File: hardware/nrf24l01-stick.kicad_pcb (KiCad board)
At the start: 2 copper layers, 48.3 x 16.3 mm, 25 parts, among them J1 USB_B_Micro, J2 SWD, SW1 SW_Push, U1 STM32L082KBUx, U2 NRF24L01_Breakout, U3 LP2985-3.3

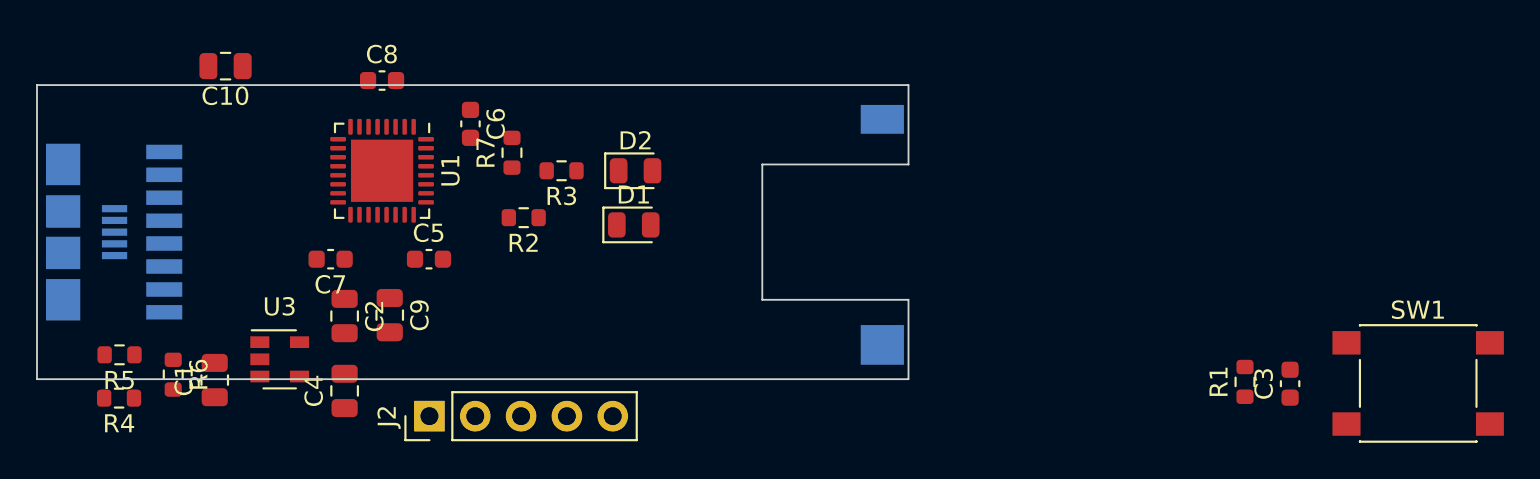
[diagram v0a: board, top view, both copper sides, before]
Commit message: Designed the rest of the PCB.
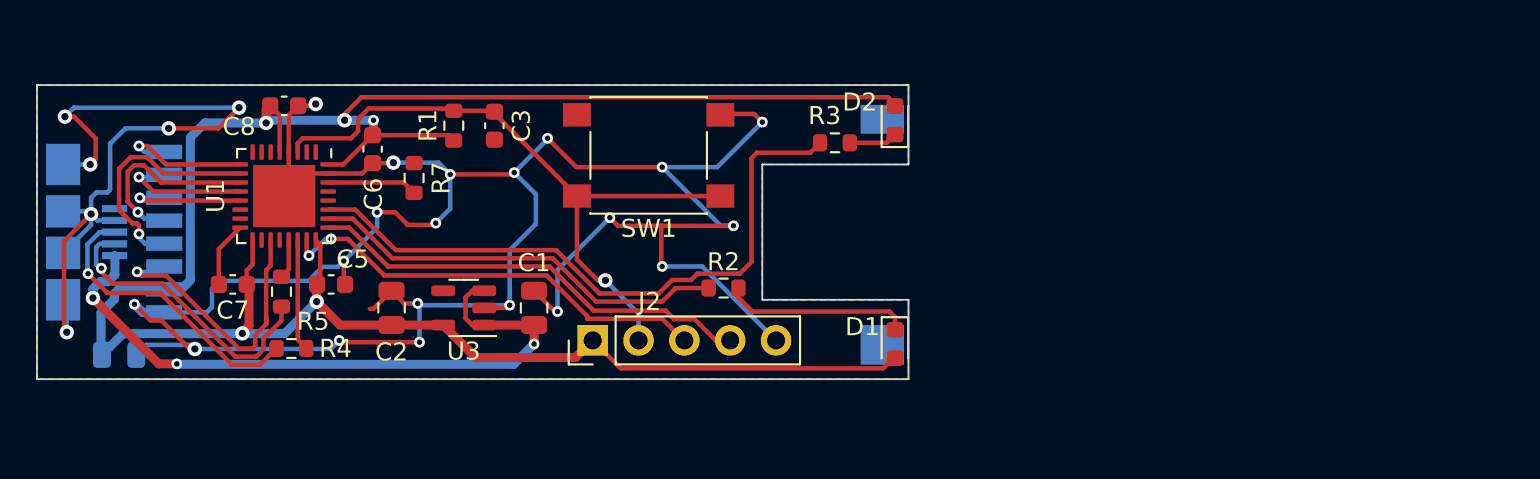
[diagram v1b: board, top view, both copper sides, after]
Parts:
- removed C4: 0.01uF, Capacitor_SMD:C_0805_2012Metric
- removed C9: 10uF, Capacitor_SMD:C_0805_2012Metric
- removed R6: 1.5K, Resistor_SMD:R_0603_1608Metric
- C10: moved to B.Cu
- D1, D2: footprint LED_SMD:LED_0805_2012Metric -> LED_SMD:LED_0603_1608Metric
- R4, R5: value 20 -> 22
- U3: value LP2985-3.3 -> MIC5504-3.3YM5
- moved C3 46.4 mm to (148.3, 46.3)
- moved R1 46.1 mm to (146.1, 46.3)
- moved SW1 44.5 mm to (156.8, 48.0), turned to 180 degrees
- moved C1 18.1 mm to (150.5, 56.4)
- moved C10 17.1 mm to (127.5, 59.0), turned to 0 degrees
- moved D1 15.9 mm to (170.5, 58.4), turned to -90 degrees
- moved R3 15.2 mm to (167.2, 47.2)
- moved D2 14.6 mm to (170.5, 46.0), turned to 90 degrees
- moved R2 11.7 mm to (161.0, 55.3)
- moved U3 10.6 mm to (146.6, 56.4), turned to 180 degrees
- moved J2 9.98 mm to (153.8, 58.2)
- moved R4 9.94 mm to (137.1, 58.6)
- moved R5 9.63 mm to (136.5, 55.5), turned to -90 degrees
- moved R7 5.60 mm to (143.8, 49.2)
- moved C5 5.60 mm to (139.2, 55.1)
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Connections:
- U1 pad 18: /~IRQ -> no_connect_(U1-Pad18)
- U1 pad 9: no_connect_(U1-Pad9) -> /~IRQ
- U3 pad 4: Net-(C4-Pad1) -> no_connect_(U3-Pad4)
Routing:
- net GND: track 0.00 -> 183.1 mm, vias 0 -> 26
- net +3V3: track 0.00 -> 127.8 mm, vias 0 -> 5
- net +5V: track 0.00 -> 36.9 mm, vias 0 -> 3
- net /~RESET: track 0.00 -> 36.8 mm, vias 0 -> 1
- net /~RX: track 0.00 -> 36.0 mm
- net /SWCLK: track 0.00 -> 24.9 mm
- net /SWDIO: track 0.00 -> 24.5 mm, vias 0 -> 2
- net /~TX: track 0.00 -> 23.3 mm
- net /CE: track 0.00 -> 16.6 mm, vias 0 -> 1
- net Net-(J1-Pad2): track 0.00 -> 16.5 mm, vias 0 -> 1
- net Net-(J1-Pad3): track 0.00 -> 16.4 mm, vias 0 -> 1
- net /~CS: track 0.00 -> 13.3 mm, vias 0 -> 1
- net /SCK: track 0.00 -> 10.9 mm, vias 0 -> 1
- net Net-(D1-Pad1): track 0.00 -> 10.4 mm
- net /~IRQ: track 0.00 -> 7.59 mm, vias 0 -> 1
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- added copper zone on B.Cu, net GND
- added copper zone on F.Cu, net GND

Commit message: Add labels for the SWD pinout.
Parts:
- moved R2 1.55 mm to (161.0, 53.8)
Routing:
- net GND: track 183.1 -> 187.5 mm, vias 26 -> 28
- net Net-(D1-Pad1): track 10.4 -> 11.9 mm
- net /~RX: track 36.0 -> 34.8 mm
- net /~TX: track 23.3 -> 23.9 mm
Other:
- board text added: "3"
- board text added: "CLK"
- board text added: "G"
- board text added: "IO"
- board text added: "~RST"
